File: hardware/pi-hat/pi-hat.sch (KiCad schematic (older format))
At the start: 39 parts, among them J1 PWR IN, J10 6-8, J11 Audio Out, J12 PWM0, J13 PWM1, J2 A-F, J3 40HAT, J4 G-M, J5 N-Q, J6 PANEL_PWR, J7 PANEL_CTL, J8 2-5, J9 WP, Q1 DMG2305UX, Q2 DMMT5401, U1 CAT24C32, U2 CM1293A, U3 CM1293A, U4 CM1293A, U5 CM1293A, U6 CM1293A, U7 CM1293A

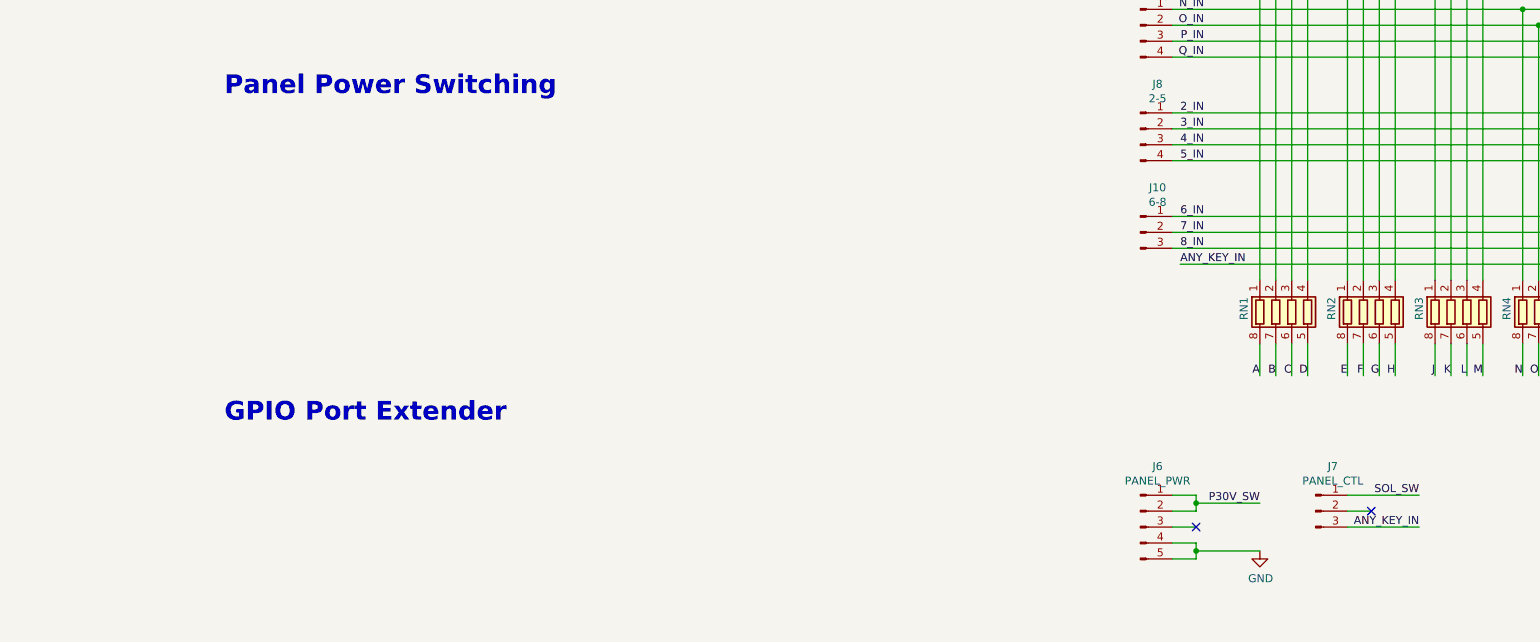
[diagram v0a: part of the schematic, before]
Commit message: panel switch fets
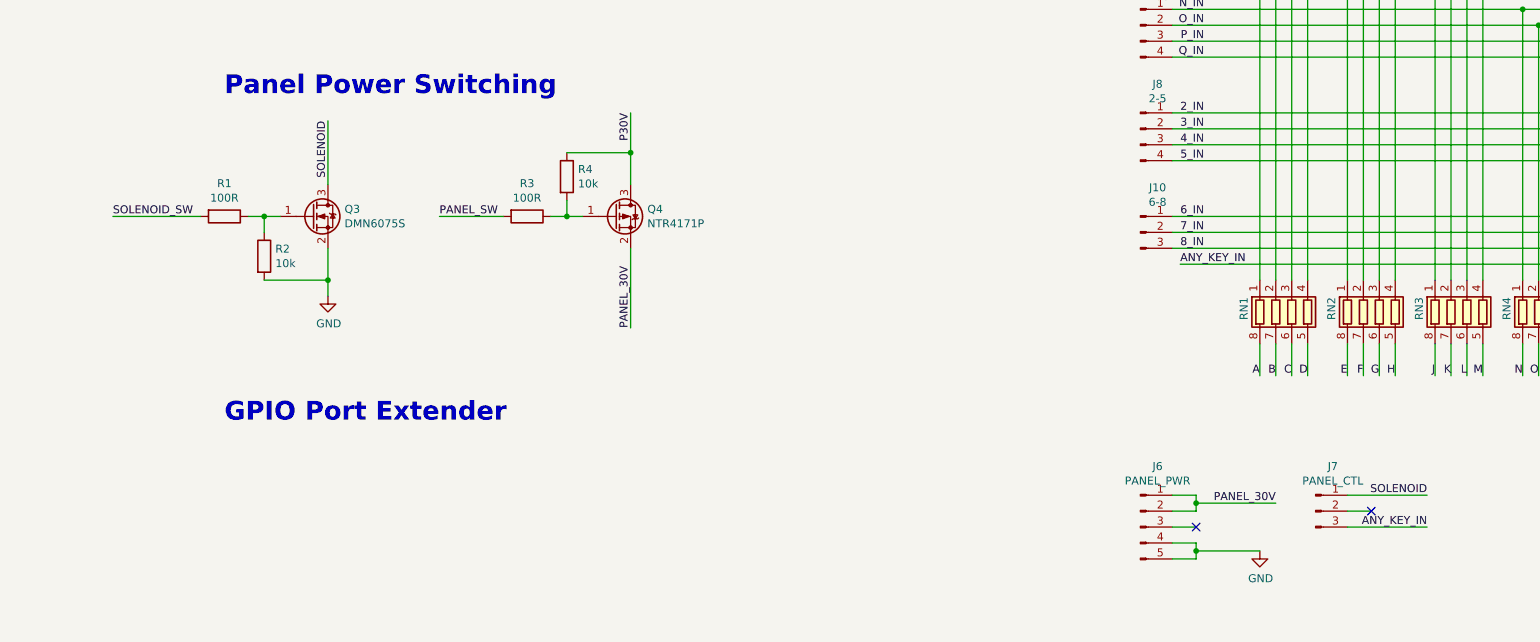
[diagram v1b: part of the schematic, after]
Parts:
- added Q3: DMN6075S, symbol Device:Q_NMOS_GSD
- added Q4: NTR4171P, symbol Device:Q_PMOS_GSD
- added R1, R3: 100R, symbol Device:R
- added R2, R4: 10k, symbol Device:R
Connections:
- net labels added: PANEL_30V, PANEL_SW, SOLENOID, SOLENOID_SW
- net labels removed: P30V_SW, SOL_SW
- wire segments 227 -> 243
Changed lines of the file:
@@
 Wire Wire Line
 	11350 7550 11350 7600
-Text Label 11750 7550 2    50   ~ 0
-P30V_SW
-Wire Wire Line
-	11350 7550 11750 7550
+Text Label 11850 7550 2    50   ~ 0
+PANEL_30V
+Wire Wire Line
+	11350 7550 11850 7550
 Wire Wire Line
 	11200 7800 11350 7800
@@
 $EndComp
 Wire Wire Line
-	12300 7500 12750 7500
-Wire Wire Line
-	12300 7700 12750 7700
+	12300 7500 12800 7500
+Wire Wire Line
+	12300 7700 12800 7700
 Wire Wire Line
 	12300 7600 12450 7600
 NoConn ~ 12450 7600
-Text Label 12750 7500 2    50   ~ 0
-SOL_SW
-Text Label 12750 7700 2    50   ~ 0
+Text Label 12800 7500 2    50   ~ 0
+SOLENOID
+Text Label 12800 7700 2    50   ~ 0
 ANY_KEY_IN
 Wire Wire Line
@@
 Text Label 4400 3050 2    50   ~ 0
 SPI_CS1
+$Comp
+L Device:Q_NMOS_GSD Q3
+U 1 1 5E8CA5D3
+P 5800 5750
+F 0 "Q3" H 6004 5796 50  0000 L CNN
+F 1 "DMN6075S" H 6004 5705 50  0000 L CNN
+F 2 "" H 6000 5850 50  0001 C CNN
+F 3 "~" H 5800 5750 50  0001 C CNN
+	1    5800 5750
+	1    0    0    -1
+$EndComp
+$Comp
+L Device:Q_PMOS_GSD Q4
+U 1 1 5E8CB29E
+P 7700 5750
+F 0 "Q4" H 7905 5796 50  0000 L CNN
+F 1 "NTR4171P" H 7905 5705 50  0000 L CNN
+F 2 "" H 7900 5850 50  0001 C CNN
+F 3 "~" H 7700 5750 50  0001 C CNN
+	1    7700 5750
+	1    0    0    -1
+$EndComp
+Wire Wire Line
+	5900 5550 5900 5150
+Text Label 5900 5150 3    50   ~ 0
+SOLENOID
+$Comp
+L power:GND #PWR017
+U 1 1 5E973E3D
+P 5900 6250
+F 0 "#PWR017" H 5900 6000 50  0001 C CNN
+F 1 "GND" H 5905 6077 50  0000 C CNN
+F 2 "" H 5900 6250 50  0001 C CNN
+F 3 "" H 5900 6250 50  0001 C CNN
+	1    5900 6250
+	1    0    0    -1
+$EndComp
+Wire Wire Line
+	5900 6250 5900 6150
+Text Label 4550 5750 0    50   ~ 0
+SOLENOID_SW
+Wire Wire Line
+	5600 5750 5500 5750
+$Comp
+L Device:R R2
+U 1 1 5E99F57D
+P 5500 6000
+F 0 "R2" H 5570 6046 50  0000 L CNN
+F 1 "10k" H 5570 5955 50  0000 L CNN
+F 2 "" V 5430 6000 50  0001 C CNN
+F 3 "~" H 5500 6000 50  0001 C CNN
+	1    5500 6000
+	1    0    0    -1
+$EndComp
+Wire Wire Line
+	5500 5850 5500 5750
+Wire Wire Line
+	5500 6150 5900 6150
+Connection ~ 5900 6150
+Wire Wire Line
+	5900 6150 5900 5950
+$Comp
+L Device:R R1
+U 1 1 5E9CB4C8
+P 5250 5750
+F 0 "R1" V 5043 5750 50  0000 C CNN
+F 1 "100R" V 5134 5750 50  0000 C CNN
+F 2 "" V 5180 5750 50  0001 C CNN
+F 3 "~" H 5250 5750 50  0001 C CNN
+	1    5250 5750
+	0    1    1    0
+$EndComp
+Wire Wire Line
+	5400 5750 5500 5750
+Connection ~ 5500 5750
+Wire Wire Line
+	5100 5750 4550 5750
+Wire Wire Line
+	7800 5550 7800 5350
+Text Label 7800 5100 3    50   ~ 0
+P30V
+Wire Wire Line
+	7800 5950 7800 6450
+Text Label 7800 6450 1    50   ~ 0
+PANEL_30V
+$Comp
+L Device:R R4
+U 1 1 5EA11609
+P 7400 5500
+F 0 "R4" H 7470 5546 50  0000 L CNN
+F 1 "10k" H 7470 5455 50  0000 L CNN
+F 2 "" V 7330 5500 50  0001 C CNN
+F 3 "~" H 7400 5500 50  0001 C CNN
+	1    7400 5500
+	1    0    0    -1
+$EndComp
+Wire Wire Line
+	7400 5350 7800 5350
+Connection ~ 7800 5350
+Wire Wire Line
+	7800 5350 7800 5100
+Wire Wire Line
+	7400 5650 7400 5750
+Wire Wire Line
+	7400 5750 7500 5750
+$Comp
+L Device:R R3
+U 1 1 5EA3050A
+P 7150 5750
+F 0 "R3" V 6943 5750 50  0000 C CNN
+F 1 "100R" V 7034 5750 50  0000 C CNN
+F 2 "" V 7080 5750 50  0001 C CNN
+F 3 "~" H 7150 5750 50  0001 C CNN
+	1    7150 5750
+	0    1    1    0
+$EndComp
+Wire Wire Line
+	7300 5750 7400 5750
+Connection ~ 7400 5750
+Wire Wire Line
+	7000 5750 6600 5750
+Text Label 6600 5750 0    50   ~ 0
+PANEL_SW
 $EndSCHEMATC

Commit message: cleanup and documentation
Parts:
- added TP?: TP_PANEL_SW, symbol Connector:TestPoint
- added TP?: TP_PANEL_30V, symbol Connector:TestPoint
- added TP?: TP_SOLENOID, symbol Connector:TestPoint
- added TP?: TP_SOLENOID_SW, symbol Connector:TestPoint
- added U8, U9: MCP23S17_SO, Package_SO:SOIC-28W_7.5x17.9mm_P1.27mm, symbol Interface_Expansion:MCP23S17_SO
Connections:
- net labels added: IO_INT, SPI_CS, WP
- net labels removed: SPI_CS0, SPI_CS1
- wire segments 243 -> 305
- no-connect marks 4 -> 12
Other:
- note added: "All Inputs are equipped with 3.3V ESD Suppression Diodes and series resistors for ESD and\ninductive coupled Transients to support the the long cable runs and close high-current\nsolenoids and incandescent bulbs.\nAll Inputs als"
- note added: "The MCP23S17 (SPI 16bit Port Extender) is used to drive and read from the Panel-IOs\nand to drive the Panel-Power FETs. This device supports an Address-Based selection mode:\nonly the Chip-Select is used for both chips; The Interrupt-Mirror-Feature is used, to only\nhave one Interrupt for all 4 Banks."
- note removed: "tbd"
- moved on the sheet: J1, J10, J12, J13, J2, J4, J5, J6, J7, J8, J9, Q3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

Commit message: footprint assignments and early board layout
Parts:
- removed J11: Audio Out, symbol Connector:Conn_Coaxial_x2
- removed TP1, TP2: wp, symbol Connector:TestPoint
- removed TP?: TP_PANEL_SW, symbol Connector:TestPoint
- removed TP?: TP_PANEL_30V, symbol Connector:TestPoint
- removed TP?: TP_SOLENOID, symbol Connector:TestPoint
- removed TP?: TP_SOLENOID_SW, symbol Connector:TestPoint
- added TP1: TP_WP, project_footprints:TestPoint_Bridge_Jumper_Pitch2.0mm, symbol Connector:TestPoint_2Pole
- J1, J2, J4: footprint (none) -> Connector_JST:JST_XH_B6B-XH-A_1x06_P2.50mm_Vertical
- J10, J7: footprint (none) -> Connector_JST:JST_XH_B3B-XH-A_1x03_P2.50mm_Vertical
- J11: renamed from J12; footprint (none) -> Connector_JST:JST_XH_B2B-XH-A_1x02_P2.50mm_Vertical
- J12: renamed from J13; footprint (none) -> Connector_JST:JST_XH_B2B-XH-A_1x02_P2.50mm_Vertical
- J5, J8: footprint (none) -> Connector_JST:JST_XH_B4B-XH-A_1x04_P2.50mm_Vertical
- J6: footprint (none) -> Connector_JST:JST_XH_B5B-XH-A_1x05_P2.50mm_Vertical
- Q2: footprint Package_TO_SOT_SMD:SOT-23-6 -> Package_TO_SOT_SMD:SOT-23-6_Handsoldering
- Q3, Q4: footprint (none) -> Package_TO_SOT_SMD:SOT-23
- R1, R2, R3, R4: footprint (none) -> Resistor_SMD:R_1206_3216Metric_Pad1.42x1.75mm_HandSolder
- R23, R24, R29, R6, R8: footprint Resistor_SMD:R_0603_1608Metric_Pad0.84x1.00mm_HandSolder -> Resistor_SMD:R_1206_3216Metric_Pad1.42x1.75mm_HandSolder
- RN1, RN2, RN3, RN4, RN5, RN6: value R_Pack04 -> EXB-38V103JV; footprint (none) -> Resistor_SMD:R_Array_Convex_4x1206
- U2, U3, U4, U5, U6, U7: footprint (none) -> Package_SO:TSOP-6_1.65x3.05mm_P0.95mm
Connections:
- net labels removed: LEFT, RIGHT
- wire segments 305 -> 301
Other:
- note added: "The HAT spec requires this EEPROM with system information\nto be in place in order to be called a HAT. It is set up as write\nprotected (WP pin held high) and can be enabled for writing by\nplacing a jumper on J9 or by bridging TP1."
- note removed: "The HAT spec requires this EEPROM with system information\nto be in place in order to be called a HAT. It is set up as write\nprotected (WP pin held high) and can be enabled for writing by\nplacing a jumper on J9 or by bridging TP1 and TP2."
- moved on the sheet: J11, J12

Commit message: first power traces
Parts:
- added TP?: TP_GND, TestPoint:TestPoint_Pad_D2.0mm, symbol Connector:TestPoint
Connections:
- net P3V3_HAT is gone; now on net P3V3: J3.1 (P3V3), U2.5 (VP), U3.5 (VP), U4.5 (VP), U5.5 (VP), U6.5 (VP), U7.5 (VP)
- net GND: now also TP?.1
- net P3V3: now also J3.17 (P3V3)
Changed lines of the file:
@@
 $EndComp
 Text Label 15750 3500 2    50   ~ 0
-P3V3_HAT
+P3V3
 Wire Wire Line
 	15400 3800 15750 3800
@@
 	15400 4150 15750 4150
 Text Label 15750 4150 2    50   ~ 0
-P3V3_HAT
+P3V3
 $Comp
 L raspberrypi_hat:CM1293A U5
@@
 	15400 5100 15750 5100
 Text Label 15750 4800 2    50   ~ 0
-P3V3_HAT
+P3V3
 $Comp
 L power:GND #PWR013
@@
 	13650 1950 13650 2200
 Text Label 15750 1550 2    50   ~ 0
-P3V3_HAT
+P3V3
 $Comp
 L power:GND #PWR012
@@
 	15400 3150 15750 3150
 Text Label 15750 2200 2    50   ~ 0
-P3V3_HAT
+P3V3
 Text Label 15750 2850 2    50   ~ 0
-P3V3_HAT
+P3V3
 $Comp
 L power:GND #PWR08
@@
 	2000 2250 800  2250
 Text Label 800  2250 0    60   ~ 0
-P3V3_HAT
+P3V3
 Wire Wire Line
 	2000 2650 800  2650
@@
 Wire Wire Line
 	5950 5000 5950 5400
+Wire Wire Line
+	2000 3050 800  3050
+Text Label 800  3050 0    50   ~ 0
+P3V3
+$Comp
+L Connector:TestPoint TP?
+U 1 1 5FDCE731
+P 9200 4400
+F 0 "TP?" V 9154 4588 50  0000 L CNN
+F 1 "TP_GND" V 9245 4588 50  0000 L CNN
+F 2 "TestPoint:TestPoint_Pad_D2.0mm" H 9400 4400 50  0001 C CNN
+F 3 "~" H 9400 4400 50  0001 C CNN
+	1    9200 4400
+	0    1    1    0
+$EndComp
+$Comp
+L power:GND #PWR?
+U 1 1 5FDD5B14
+P 8850 4400
+F 0 "#PWR?" H 8850 4150 50  0001 C CNN
+F 1 "GND" V 8855 4272 50  0000 R CNN
+F 2 "" H 8850 4400 50  0001 C CNN
+F 3 "" H 8850 4400 50  0001 C CNN
+	1    8850 4400
+	0    1    1    0
+$EndComp
+Wire Wire Line
+	8850 4400 9200 4400
 $EndSCHEMATC

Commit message: add audio section with split gnd and 3v3
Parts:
- removed TP1: TP_WP, project_footprints:TestPoint_Bridge_Jumper_Pitch2.0mm, symbol Connector:TestPoint_2Pole
- added C1, C10, C11, C14, C16, C3, C5: 10uF, Capacitor_SMD:C_0805_2012Metric, symbol Device:CP_Small
- added C12, C15, C17, C2, C4, C6: .1uF, Capacitor_SMD:C_0805_2012Metric, symbol Device:C_Small
- added C13, C7, C8, C9: 2.2uF, Capacitor_SMD:C_0805_2012Metric, symbol Device:C_Small
- added J13: KLPX-0848A-2-B, project_footprints:KLPX_RCA, symbol Connector:Conn_Coaxial
- added J14: KLPX-0848A-2-R, project_footprints:KLPX_RCA, symbol Connector:Conn_Coaxial
- added JP?: Jumper_NC_Small, symbol Device:Jumper_NC_Small
- added R10, R11: 3.9K, Resistor_SMD:R_0805_2012Metric, symbol Device:R
- added R12, R13: 100R, Resistor_SMD:R_0805_2012Metric, symbol Device:R
- added R5: 10k, Resistor_SMD:R_0805_2012Metric, symbol Device:R
- added R7, R9: 470R, Resistor_SMD:R_0805_2012Metric, symbol Device:R
- added U10, U11: L78L33_SOT89, Package_TO_SOT_SMD:SOT-89-3, symbol Regulator_Linear:L78L33_SOT89
- added U12: PCM5122PW, Package_SO:TSSOP-28_4.4x9.7mm_P0.65mm, symbol Audio:PCM5122PW
- R1, R2, R23, R24, R29, R3, R4, R6, R8: footprint Resistor_SMD:R_1206_3216Metric_Pad1.42x1.75mm_HandSolder -> Resistor_SMD:R_0805_2012Metric
- RN1, RN2, RN3, RN4, RN5, RN6: footprint Resistor_SMD:R_Array_Convex_4x1206 -> Resistor_SMD:R_Array_Convex_4x0603
- gave numbers to parts that had none: 1
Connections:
- net GND: now also C14.2, C15.2, C16.2, C17.2, C3.2, C4.2, C5.2, C6.2, JP?.1, R13.2, R5.1, U10.2 (GND), U12.17 (MODE1), U12.27 (DGND)
- net I2C_SCL: now also R11.2, U12.12 (SCL/MC/ATT1)
- net I2C_SDA: now also R10.2, U12.11 (SDA/MOSI/ATT2)
- net P3V3: now also C14.1, C15.1, C16.1, C17.1, C3.1, C4.1, R10.1, R11.1, R12.2, U10.1 (OUT), U12.18 (MODE2/MS), U12.25 (XSMT), U12.28 (DVDD); no longer J3.1 (P3V3), J3.17 (P3V3)
- net P5V: now also U10.3 (IN), U11.3 (IN)
- net PCM_CLK: now also U12.21 (BCK)
- net PCM_FS: now also U12.23 (LRCK)
- net SPI_CS: now also J3.24 (BCM8), R5.2; no longer J3.16 (BCM23)
- net IO_INT_B: now reaches J3.22 (BCM25)
- net IO_INT_B: now also U9.20 (INTA)
- net ID_SC_EEPROM renamed ID_SCL
- net ID_SD_EEPROM renamed ID_SDA
- net IO_INT renamed IO_INT_A
- net IO_INT_A: no longer U9.20 (INTA)
- net PCM_DOUT renamed PCM_DATA
- net PCM_DATA: now also U12.22 (DIN)
- new net ADR1: R12.1, U12.24 (ADR1/MISO/FMT)
- new net ADR2: R13.1, U12.16 (ADR2/GPIO2/DOUT)
- new net CAPM: C7.2, U12.4 (CAPM)
- new net CAPP: C7.1, U12.2 (CAPP)
- new net DAC_SYSCLK: U12.20 (SCK)
- new net GNDA: C1.2, C10.2, C11.2, C12.2, C13.2, C2.2, C8.1, C9.1, J13.2 (Ext), J14.2 (Ext), JP?.2, U11.2 (GND), U12.3 (CPGND), U12.9 (AGND)
- new net LDOO: C5.1, C6.1, U12.26 (LDOO)
- new net L_CHAN: C13.1, J13.1 (In), R7.1
- new net L_RAW: R7.2, U12.6 (OUTL)
- new net P3V3A: C1.1, C11.1, C12.1, C2.1, U11.1 (OUT), U12.1 (CPVDD), U12.8 (AVDD)
- new net R_CHAN: C9.2, J14.1 (In), R9.1
- new net R_RAW: R9.2, U12.7 (OUTR)
- new net VCOM: C10.1, U12.10 (VCOM/DEMP)
- new net VNRG: C8.2, U12.5 (VNEG)
- no-connect marks 12 -> 32
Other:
- note added: "(!) Remove Groundplane (!)\nbeween Output-Channels0\nto avoid crosstalk"
- note added: "Decoupling between\nAVDD / AGND"
- note added: "Decoupling between\nCPVDD / CPGND"
- note added: "Decoupling between\nDVDD / DGND"
- note added: "Decoupling between\nLDO0 / DGND"
- note added: "GNDA and GND are to be joined\nin a start-ground point"
- note added: "The System-Clock SCK is generated with a PLL internally.\nAlternatively one can add 2 extra Oscillatory to enhance \nthe frequency stability. They are controlled by GPIO 3/6 \nfrom the Linux-Driver."
- note removed: "ID I2C Pullup Resistors"
- note removed: "These are just pullup resistors for the I2C bus on the EEPROM.\nThe resistor values are per the HAT spec."
- moved on the sheet: H1, H2, H3, H4, J11, J12, R6, R8, TP2, U8

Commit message: route io protection
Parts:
- JP1: renamed from JP?; footprint (none) -> Jumper:SolderJumper-2_P1.3mm_Bridged2Bar_RoundedPad1.0x1.5mm
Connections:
- net E_IN: now also RN2.2 (R2.1), U3.1 (CH1); no longer RN2.1 (R1.1), U3.6 (CH4)
- net F_IN: now also RN2.1 (R1.1), U3.3 (CH2); no longer RN2.2 (R2.1), U3.4 (CH3)
- net G_IN: now also U3.6 (CH4); no longer U3.3 (CH2)
- net H_IN: now also U3.4 (CH3); no longer U3.1 (CH1)
- net P3V3: no longer R29.1, R6.1, R8.1, U1.8 (VCC)
- net P3V3_HAT: now reaches J3.17 (P3V3)
- net P3V3_HAT: now also R29.1, R6.1, R8.1, U1.8 (VCC)
- no-connect marks 32 -> 31
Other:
- moved on the sheet: R29
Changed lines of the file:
@@
 Comment4 ""
 $EndDescr
-Text Label 2800 7000 2    60   ~ 0
-P3V3
+Text Label 3000 7000 2    60   ~ 0
+P3V3_HAT
 $Comp
 L raspberrypi_hat:CAT24C32 U1
@@
 L Device:R R29
 U 1 1 58E19E51
-P 1550 6250
-F 0 "R29" V 1630 6250 50  0000 C CNN
-F 1 "10K" V 1550 6250 50  0000 C CNN
-F 2 "Resistor_SMD:R_0805_2012Metric" V 1480 6250 50  0001 C CNN
-F 3 "" H 1550 6250 50  0001 C CNN
-	1    1550 6250
+P 1400 6250
+F 0 "R29" V 1480 6250 50  0000 C CNN
+F 1 "10K" V 1400 6250 50  0000 C CNN
+F 2 "Resistor_SMD:R_0805_2012Metric" V 1330 6250 50  0001 C CNN
+F 3 "" H 1400 6250 50  0001 C CNN
+	1    1400 6250
 	-1   0    0    1
 $EndComp
-Text Label 2400 5350 2    60   ~ 0
-P3V3
-Wire Wire Line
-	2100 5350 2400 5350
+Text Label 2550 5350 2    60   ~ 0
+P3V3_HAT
+Wire Wire Line
+	2100 5350 2550 5350
 Wire Wire Line
 	2100 5350 2100 5450
@@
 Wire Wire Line
 	2100 6250 2100 6350
-Text Label 1800 6550 2    60   ~ 0
-P3V3
-Wire Wire Line
-	1800 6550 1550 6550
-Wire Wire Line
-	1550 6550 1550 6400
+Text Label 1900 6550 2    60   ~ 0
+P3V3_HAT
+Wire Wire Line
+	1900 6550 1400 6550
+Wire Wire Line
+	1400 6550 1400 6400
 Wire Wire Line
 	1050 5650 1050 5750
@@
 	1950 7000 2000 7000
 Wire Wire Line
-	2450 7000 2800 7000
+	2450 7000 3000 7000
 Wire Wire Line
 	1300 5750 1300 5850
@@
 	1300 5650 1600 5650
 Wire Wire Line
-	1550 6050 1600 6050
-Wire Wire Line
-	1550 6050 1550 6100
+	1400 6050 1600 6050
+Wire Wire Line
+	1400 6050 1400 6100
 Wire Wire Line
 	950  6150 950  6200
@@
 $EndComp
 Wire Wire Line
-	11150 2050 12350 2050
-Wire Wire Line
 	13650 2600 13650 2850
 Wire Wire Line
@@
 	11900 1750 11900 5200
 Wire Wire Line
-	11150 1950 12250 1950
-Wire Wire Line
 	12000 1850 12000 5200
-Wire Wire Line
-	12250 5200 12250 1950
-Connection ~ 12250 1950
-Wire Wire Line
-	12250 1950 13650 1950
-Wire Wire Line
-	12350 5200 12350 2050
-Connection ~ 12350 2050
-Wire Wire Line
-	12350 2050 13550 2050
+Connection ~ 12350 1950
 Wire Wire Line
 	12450 5200 12450 2400
@@
 Text Label 14750 5800 0    50   ~ 0
 ANY_KEY
-Connection ~ 12450 2400
-Connection ~ 12550 2500
 Connection ~ 11700 1550
 Connection ~ 11800 1650
-Connection ~ 11900 1750
-Connection ~ 12000 1850
-Wire Wire Line
-	13550 2050 13550 2300
-Wire Wire Line
-	13650 1950 13650 2200
 Text Label 15750 1550 2    50   ~ 0
 P3V3
@@
 	15400 1550 15750 1550
 Wire Wire Line
-	12550 2500 14800 2500
-Wire Wire Line
-	12450 2400 14800 2400
-Wire Wire Line
-	12000 1850 14800 1850
-Wire Wire Line
-	11900 1750 14800 1750
-Wire Wire Line
 	11800 1650 14800 1650
 Wire Wire Line
@@
 Wire Wire Line
 	13650 2850 14800 2850
-Wire Wire Line
-	13550 2300 14800 2300
-Wire Wire Line
-	13650 2200 14800 2200
 $Comp
 L raspberrypi_hat:CM1293A U2
@@
 Text Label 950  6050 0    50   ~ 0
 WP
-Connection ~ 1550 6050
+Connection ~ 1400 6050
 Wire Wire Line
 	7850 4950 7850 5400
@@
 Text Label 7150 2600 2    60   ~ 0
 P5V_HAT
-$Comp
-L raspberrypi_hat:OX40HAT J3
-U 1 1 58DFC771
-P 2600 2250
-F 0 "J3" H 2950 2350 50  0000 C CNN
-F 1 "40HAT" H 2300 2350 50  0000 C CNN
-F 2 "Connector_PinSocket_2.54mm:PinSocket_2x20_P2.54mm_Vertical" H 2600 2450 50  0001 C CNN
-F 3 "" H 1900 2250 50  0000 C CNN
-	1    2600 2250
-	1    0    0    -1
-$EndComp
 Text Notes 850  1250 0    100  ~ 0
 This is based on the official Raspberry Pi spec to be able to call an extension board a HAT.\nhttps://github.com/raspberrypi/hats/blob/master/designguide.md
@@
 	9400 5150 9650 5150
 NoConn ~ 2000 2250
-NoConn ~ 2000 3050
 Text Label 9650 5150 2    50   ~ 0
 P3V3
@@
 VNRG
 Wire Wire Line
-	950  6050 1550 6050
+	950  6050 1400 6050
 $Comp
 L power:GNDA #PWR0101
@@
 PWM1
 $Comp
-L Device:Jumper_NC_Small JP?
+L Device:Jumper_NC_Small JP1
 U 1 1 5E1ADCE1
 P 9250 4300
-F 0 "JP?" H 9250 4421 50  0001 C CNN
+F 0 "JP1" H 9250 4421 50  0001 C CNN
 F 1 "Jumper_NC_Small" H 9250 4421 50  0001 C CNN
-F 2 "" H 9250 4300 50  0001 C CNN
+F 2 "Jumper:SolderJumper-2_P1.3mm_Bridged2Bar_RoundedPad1.0x1.5mm" H 9250 4300 50  0001 C CNN
 F 3 "~" H 9250 4300 50  0001 C CNN
 	1    9250 4300
@@
 Wire Wire Line
 	9450 4300 9350 4300
+$Comp
+L raspberrypi_hat:OX40HAT J3
+U 1 1 58DFC771
+P 2600 2250
+F 0 "J3" H 2950 2350 50  0000 C CNN
+F 1 "40HAT" H 2300 2350 50  0000 C CNN
+F 2 "Connector_PinSocket_2.54mm:PinSocket_2x20_P2.54mm_Vertical" H 2600 2450 50  0001 C CNN
+F 3 "" H 1900 2250 50  0000 C CNN
+	1    2600 2250
+	1    0    0    -1
+$EndComp
+Wire Wire Line
+	2000 3050 800  3050
+Text Label 800  3050 0    50   ~ 0
+P3V3_HAT
+Connection ~ 12000 1850
+Wire Wire Line
+	12000 1850 14800 1850
+Connection ~ 11900 1750
+Wire Wire Line
+	11900 1750 14800 1750
+Wire Wire Line
+	12350 1950 13650 1950
+Wire Wire Line
+	11150 1950 12350 1950
+Wire Wire Line
+	11150 2050 12250 2050
+Wire Wire Line
+	12350 1950 12350 5200
+Wire Wire Line
+	12250 2050 12250 5200
+Connection ~ 12250 2050
+Wire Wire Line
+	12250 2050 13550 2050
+Wire Wire Line
+	14800 2400 13550 2400
+Wire Wire Line
+	13550 2050 13550 2400
+Wire Wire Line
+	14800 2500 13650 2500
+Wire Wire Line
+	13650 1950 13650 2500
+Wire Wire Line
+	14800 2200 12450 2200
+Wire Wire Line
+	12450 2200 12450 2400
+Connection ~ 12450 2400
+Wire Wire Line
+	12550 2500 12550 2300
+Wire Wire Line
+	12550 2300 14800 2300
+Connection ~ 12550 2500
 $EndSCHEMATC
